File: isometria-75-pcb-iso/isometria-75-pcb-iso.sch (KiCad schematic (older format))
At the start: 26 parts, among them J101 USB, J102 SPI, J103 Conn_01x06_Male, Q101 AO3400A, SW101 RST, SW102 BOOT, U101 XC6206P332MR, U102 STM32F072CBTx

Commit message: major schematic/pcb rework
rewired SPI, added SPI CS/IRQ/RES pins, rewired part of the matrix in the process
changed to a larger header for SPI
added a divider for input voltage sensing
removed extension header due to a lack of remaining unused GPIOs
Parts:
- removed J103: Conn_01x06_Male, Connector_PinHeader_2.54mm:PinHeader_1x06_P2.54mm_Vertical, symbol Connector:Conn_01x06_Male
- added C113: 100n, Capacitor_SMD:C_0402_1005Metric, symbol Device:C_Small
- added R104, R105: 50k, Resistor_SMD:R_0402_1005Metric, symbol Device:R_Small
- J103: renamed from J102; footprint Connector_JST:JST_SH_SM06B-SRSS-TB_1x06-1MP_P1.00mm_Horizontal -> Connector_JST:JST_SH_SM08B-SRSS-TB_1x08-1MP_P1.00mm_Horizontal; symbol Connector_Generic:Conn_01x06 -> Connector_Generic:Conn_01x08
- renumbered C113 to C114, R104 to R106, R105 to R107
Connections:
- net PB4 is gone; now on net ROW1: U102.40 (PB4)
- net PB5 is gone; now on net ROW2: U102.41 (PB5)
- net PB6_TX1 is gone; now on net ROW3: U102.42 (PB6)
- net PB7_RX1 is gone; now on net ROW4: U102.43 (PB7)
- net +5V: now also J103.8 (Pin_8), R104.1; no longer J103.6 (Pin_6)
- net COL10: now also U102.5 (PF0); no longer U102.12 (PA2)
- net COL11: now also U102.6 (PF1); no longer U102.13 (PA3)
- net COL12: now also U102.10 (PA0); no longer U102.18 (PB0)
- net COL8: now also U102.46 (PB9); no longer U102.5 (PF0)
- net COL9: now also U102.2 (PC13); no longer U102.6 (PF1)
- net GND: now also J103.4 (Pin_4), C113.1, R105.2; no longer J103.1 (Pin_1)
- net ROTA: now also U102.4 (PC15); no longer U102.11 (PA1)
- net ROTB: now also U102.3 (PC14); no longer U102.10 (PA0)
- net ROW1: no longer U102.45 (PB8)
- net ROW2: no longer U102.46 (PB9)
- net ROW3: no longer U102.2 (PC13)
- net ROW4: no longer U102.3 (PC14)
- net ROW5: now also U102.45 (PB8); no longer U102.4 (PC15)
- net SPI_MISO: now also J103.6 (Pin_6); no longer J103.4 (Pin_4)
- net SPI_MOSI: now also J103.7 (Pin_7); no longer J103.5 (Pin_5)
- net SPI_SCK: now also J103.5 (Pin_5); no longer J103.3 (Pin_3)
- net sense_charge: now reaches C114.1, R106.2, R107.1, U102.19 (PB1)
- net BOOT: now reaches C112.1, R103.1, SW102.2, U102.44 (BOOT0)
- net RST: now reaches C110.1, SW101.2, U102.7 (NRST)
- net VDDA: now reaches C111.1, R102.2, U102.9 (VDDA)
- net SPI_NSS renamed SPI_CS
- net SPI_CS: now also J103.3 (Pin_3); no longer J103.2 (Pin_2)
- net Vsense renamed chgsense
- new net SPI_IRQ: J103.2 (Pin_2), U102.12 (PA2)
- new net SPI_RES: J103.1 (Pin_1), U102.13 (PA3)
- new net sense_battV: C113.2, R104.2, R105.1, U102.18 (PB0)
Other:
- moved on the sheet: C114, R106, R107

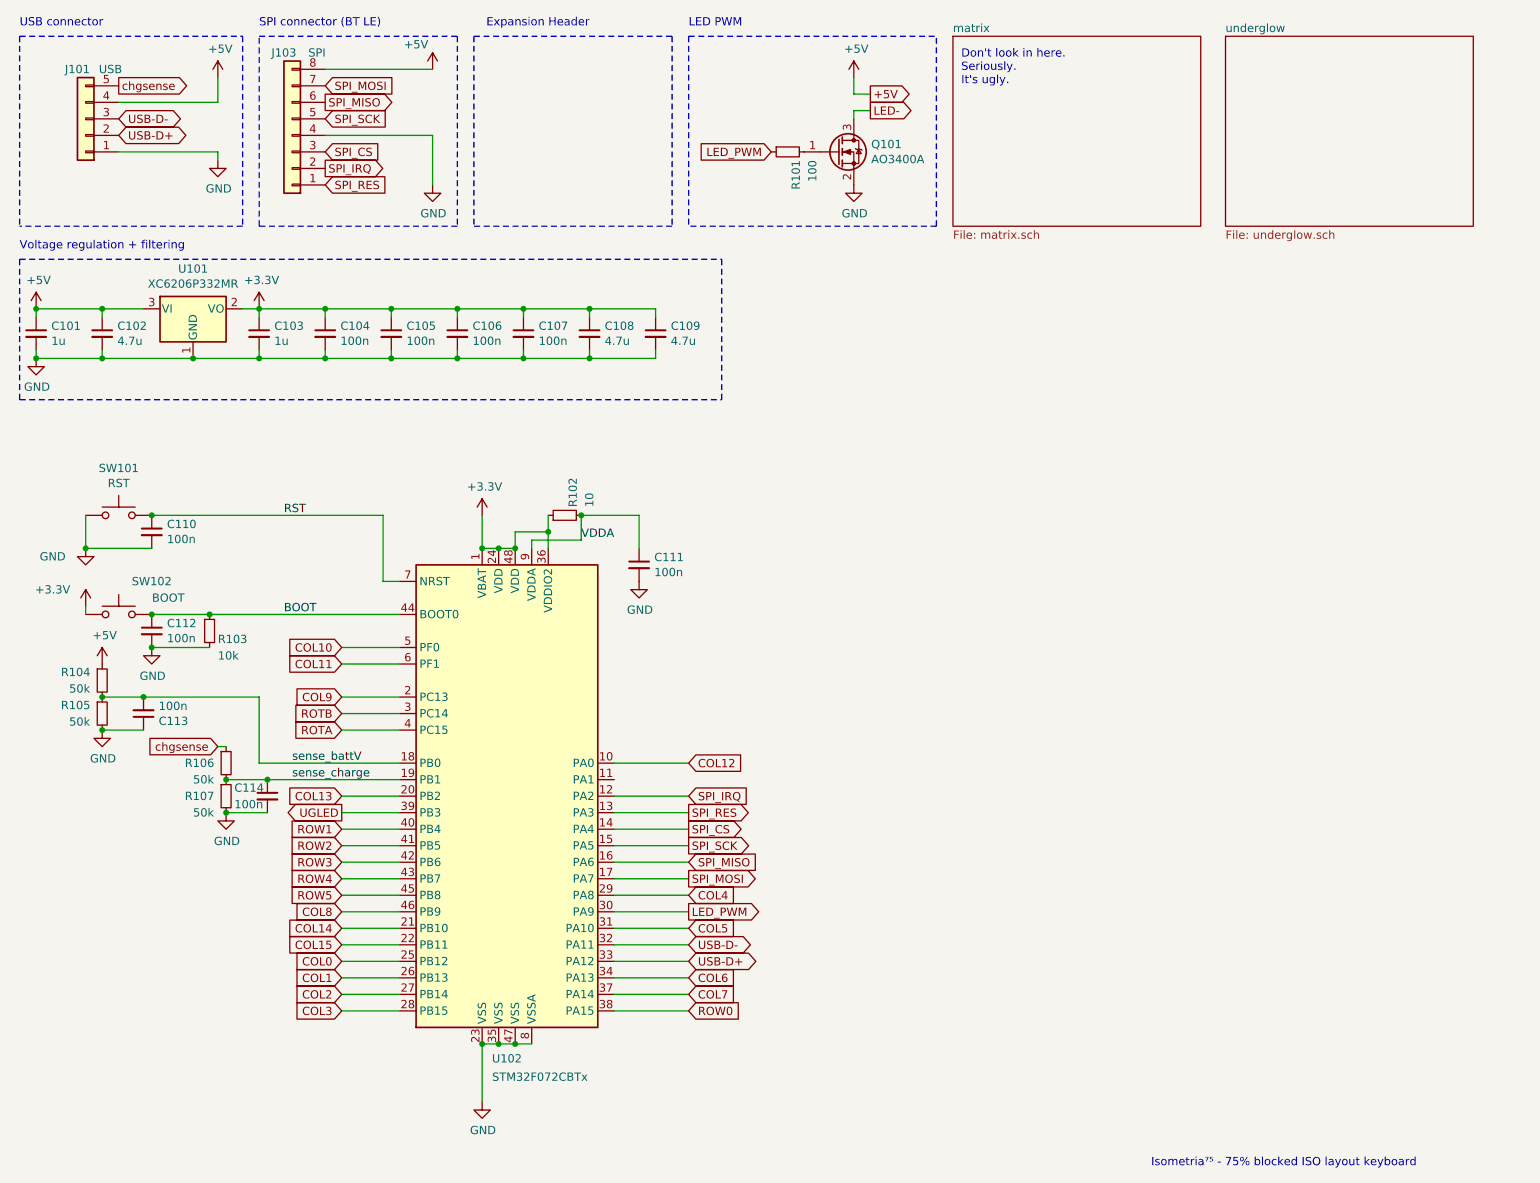
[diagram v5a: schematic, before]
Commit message: added capacity, rerouted power traces
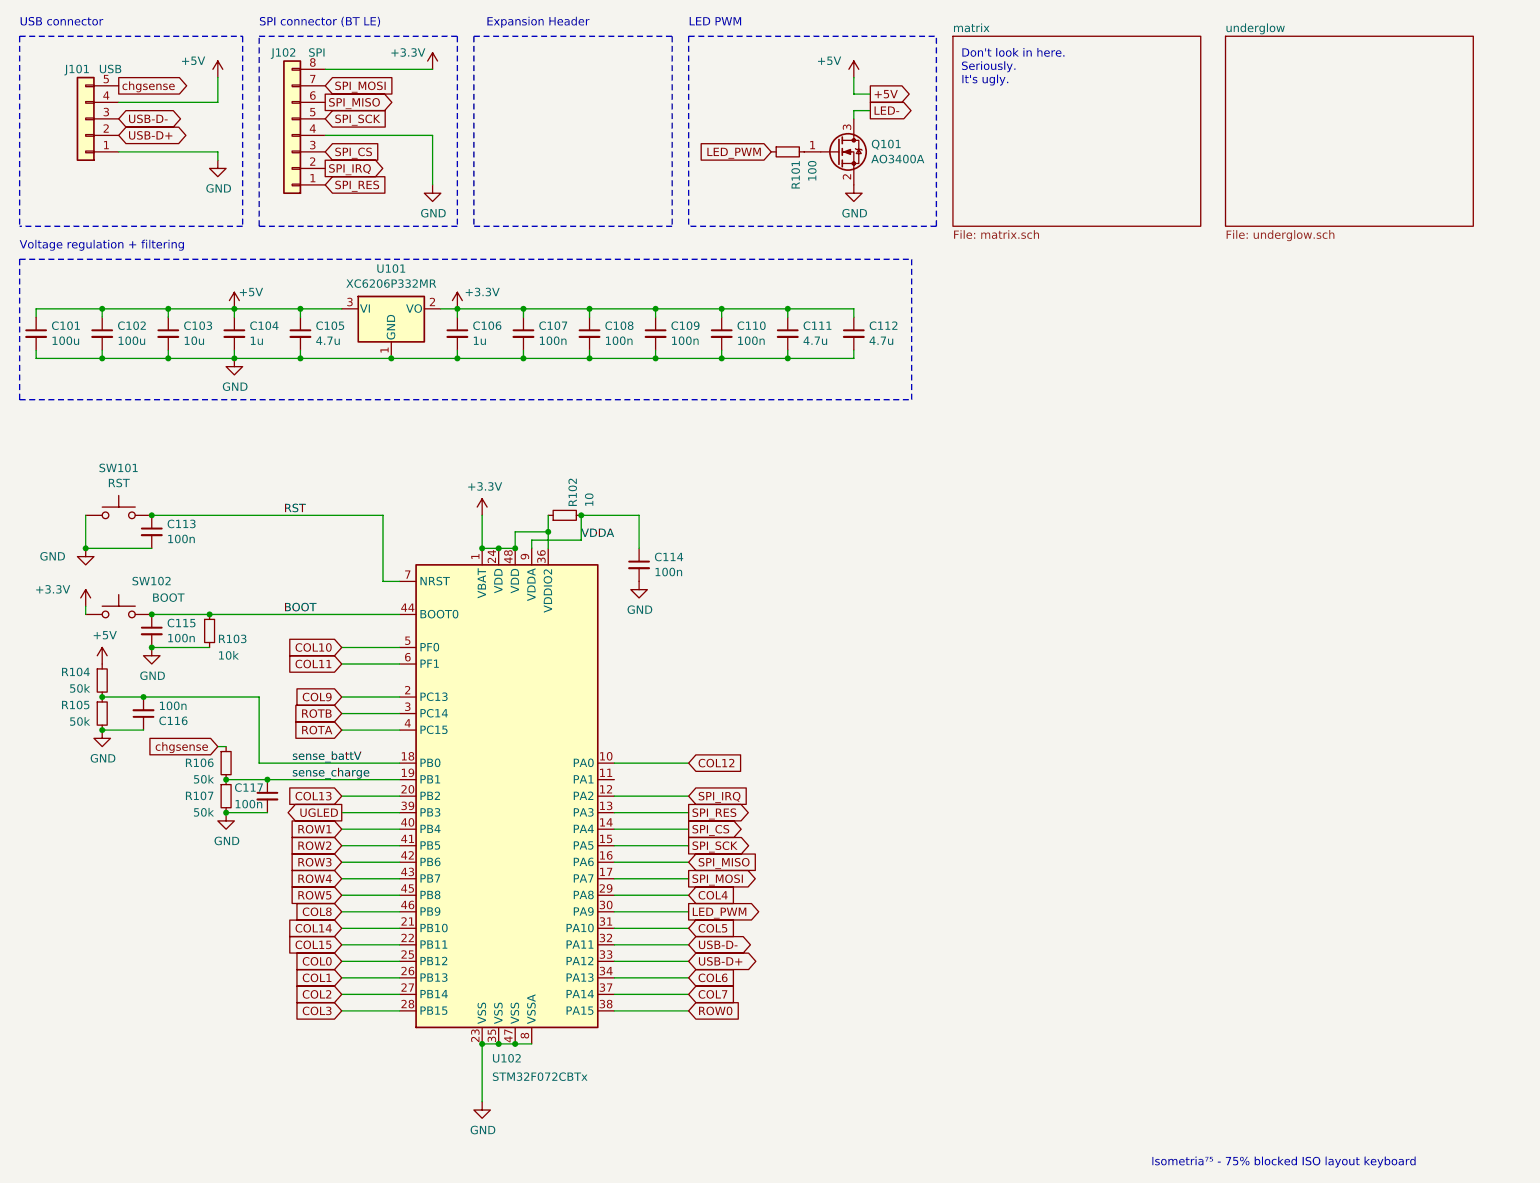
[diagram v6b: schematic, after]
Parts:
- added C101, C102: 100u, Capacitor_Tantalum_SMD:CP_EIA-3528-21_Kemet-B, symbol Device:C_Small
- added C103: 10u, Capacitor_Tantalum_SMD:CP_EIA-3216-18_Kemet-A, symbol Device:C_Small
- renumbered C101 to C104, C102 to C105, C103 to C106, C104 to C107, C105 to C108, C106 to C109, C107 to C110, C108 to C111, C109 to C112, C110 to C113, C111 to C114, C112 to C115, C113 to C116, C114 to C117, J103 to J102
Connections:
- net +3V3: now also J102.8 (Pin_8)
- net +5V: now also C101.1, C102.1, C103.1; no longer J102.8 (Pin_8)
- net GND: now also C101.2, C102.2, C103.2
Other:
- moved on the sheet: C104, C105, C106, C107, C108, C109, C110, C111, C112, U101

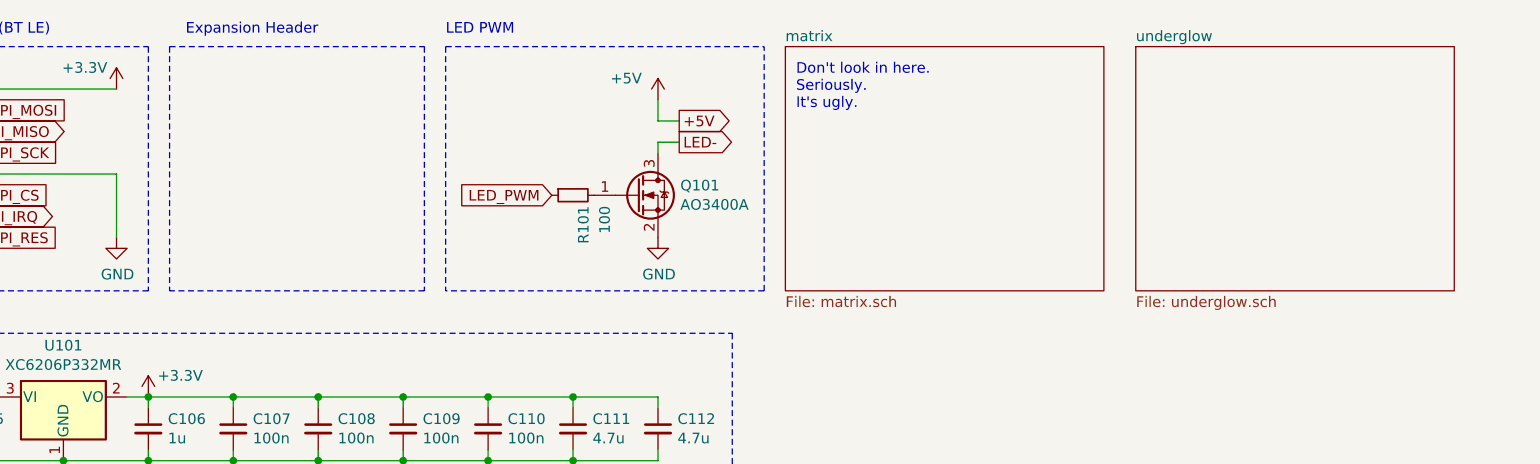
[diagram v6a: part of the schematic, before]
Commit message: deleted unused text in the schematic
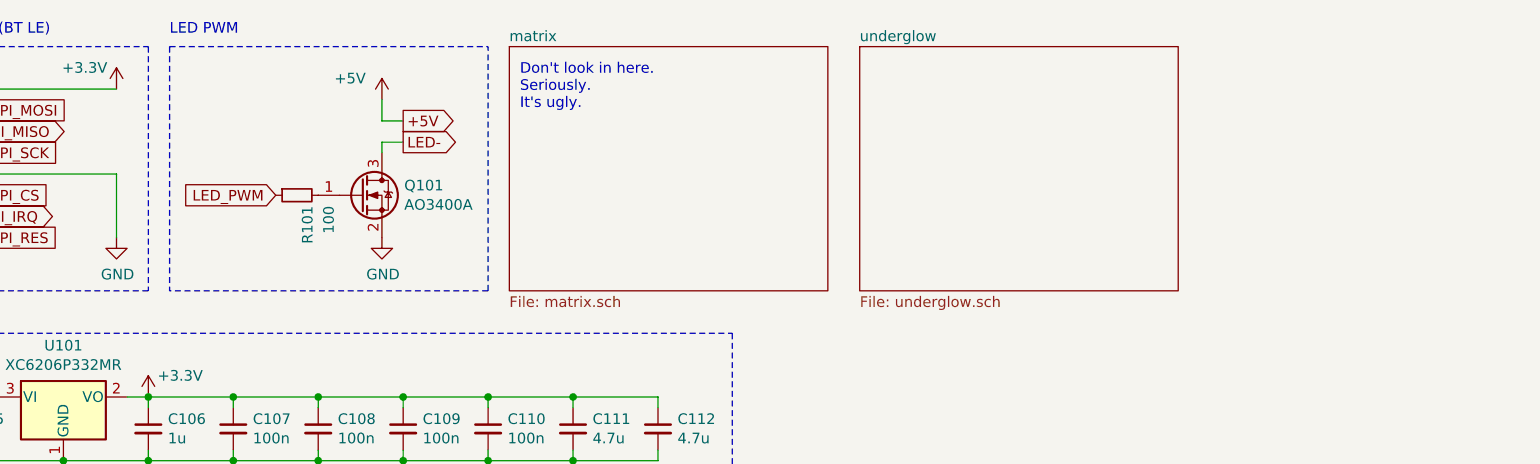
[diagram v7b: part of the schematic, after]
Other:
- note removed: "Expansion Header"
- moved on the sheet: Q101, R101
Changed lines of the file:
@@
 Connection ~ 950  3750
 $Sheet
-S 6200 650  1500 1150
+S 4900 650  1500 1150
 U 5E64D9E7
 F0 "matrix" 50
@@
 L power:+5V #PWR0103
 U 1 1 5E658CC9
-P 5600 900
-F 0 "#PWR0103" H 5600 750 50  0001 C CNN
-F 1 "+5V" H 5450 1000 50  0000 C CNN
-F 2 "" H 5600 900 50  0001 C CNN
-F 3 "" H 5600 900 50  0001 C CNN
-	1    5600 900
-	1    0    0    -1
-$EndComp
-Text GLabel 5700 1000 2    50   Output ~ 0
+P 4300 900
+F 0 "#PWR0103" H 4300 750 50  0001 C CNN
+F 1 "+5V" H 4150 1000 50  0000 C CNN
+F 2 "" H 4300 900 50  0001 C CNN
+F 3 "" H 4300 900 50  0001 C CNN
+	1    4300 900
+	1    0    0    -1
+$EndComp
+Text GLabel 4400 1000 2    50   Output ~ 0
 +5V
-Text GLabel 5700 1100 2    50   Output ~ 0
+Text GLabel 4400 1100 2    50   Output ~ 0
 LED-
 Wire Wire Line
-	5600 900  5600 1000
-Wire Wire Line
-	5600 1000 5700 1000
+	4300 900  4300 1000
+Wire Wire Line
+	4300 1000 4400 1000
 $Comp
 L Device:Q_NMOS_GSD Q101
 U 1 1 5E71ADB0
-P 5500 1350
-F 0 "Q101" H 5705 1396 50  0000 L CNN
-F 1 "AO3400A" H 5705 1305 50  0000 L CNN
-F 2 "Package_TO_SOT_SMD:SOT-23" H 5700 1450 50  0001 C CNN
-F 3 "https://datasheet.lcsc.com/szlcsc/Alpha-Omega-Semicon-AOS-AO3400A_C20917.pdf" H 5500 1350 50  0001 C CNN
-	1    5500 1350
-	1    0    0    -1
-$EndComp
-Wire Wire Line
-	5600 1100 5600 1150
-Wire Wire Line
-	5600 1100 5700 1100
+P 4200 1350
+F 0 "Q101" H 4405 1396 50  0000 L CNN
+F 1 "AO3400A" H 4405 1305 50  0000 L CNN
+F 2 "Package_TO_SOT_SMD:SOT-23" H 4400 1450 50  0001 C CNN
+F 3 "https://datasheet.lcsc.com/szlcsc/Alpha-Omega-Semicon-AOS-AO3400A_C20917.pdf" H 4200 1350 50  0001 C CNN
+	1    4200 1350
+	1    0    0    -1
+$EndComp
+Wire Wire Line
+	4300 1100 4300 1150
+Wire Wire Line
+	4300 1100 4400 1100
 $Comp
 L power:GND #PWR0106
 U 1 1 5E721452
-P 5600 1550
-F 0 "#PWR0106" H 5600 1300 50  0001 C CNN
-F 1 "GND" H 5605 1377 50  0000 C CNN
-F 2 "" H 5600 1550 50  0001 C CNN
-F 3 "" H 5600 1550 50  0001 C CNN
-	1    5600 1550
+P 4300 1550
+F 0 "#PWR0106" H 4300 1300 50  0001 C CNN
+F 1 "GND" H 4305 1377 50  0000 C CNN
+F 2 "" H 4300 1550 50  0001 C CNN
+F 3 "" H 4300 1550 50  0001 C CNN
+	1    4300 1550
 	1    0    0    -1
 $EndComp
@@
 L Device:R_Small R101
 U 1 1 5E6454D0
-P 5200 1350
-F 0 "R101" H 5250 1300 50  0000 L CNN
-F 1 "100" H 5250 1200 50  0000 L CNN
-F 2 "Resistor_SMD:R_0402_1005Metric" H 5200 1350 50  0001 C CNN
-F 3 "~" H 5200 1350 50  0001 C CNN
-	1    5200 1350
+P 3900 1350
+F 0 "R101" H 3950 1300 50  0000 L CNN
+F 1 "100" H 3950 1200 50  0000 L CNN
+F 2 "Resistor_SMD:R_0402_1005Metric" H 3900 1350 50  0001 C CNN
+F 3 "~" H 3900 1350 50  0001 C CNN
+	1    3900 1350
 	0    -1   1    0
 $EndComp
-Text GLabel 5100 1350 0    50   Input ~ 0
+Text GLabel 3800 1350 0    50   Input ~ 0
 LED_PWM
 Text GLabel 4600 5950 2    50   Output ~ 0
@@
 	550  2850 550  2000
 Wire Notes Line style solid
-	6100 1800 4600 1800
-Wire Notes Line style solid
-	4600 650  6100 650
+	4800 1800 3300 1800
+Wire Notes Line style solid
+	3300 650  4800 650
 Text Notes 550  600  0    50   ~ 0
 USB connector
@@
 Text Notes 550  1950 0    50   ~ 0
 Voltage regulation + filtering
-Text Notes 4600 600  0    50   ~ 0
+Text Notes 3300 600  0    50   ~ 0
 LED PWM
 Wire Notes Line style solid
@@
 	3200 650  3200 1800
 Wire Notes Line style solid
-	4600 650  4600 1800
-Wire Notes Line style solid
-	6100 1800 6100 650
+	3300 650  3300 1800
+Wire Notes Line style solid
+	4800 1800 4800 650
 Wire Notes Line style solid
 	5950 2000 5950 2850
@@
 Wire Wire Line
 	4600 5850 4150 5850
-Text Notes 6250 950  0    50   ~ 0
+Text Notes 4950 950  0    50   ~ 0
 Don't look in here.\nSeriously. \nIt's ugly.\n
 Text Notes 7400 7500 0    50   ~ 0
@@
 	2500 5950 2850 5950
 $Sheet
-S 7850 650  1500 1150
+S 6550 650  1500 1150
 U 5E6E13F7
 F0 "underglow" 50
@@
 Wire Wire Line
 	2500 5750 2850 5750
-Wire Notes Line style solid
-	3300 650  4500 650
-Wire Notes Line style solid
-	4500 1800 3300 1800
-Wire Notes Line style solid
-	4500 650  4500 1800
-Wire Notes Line style solid
-	3300 650  3300 1800
-Text Notes 4000 600  2    50   ~ 0
-Expansion Header
 Wire Wire Line
 	4150 5450 4600 5450
